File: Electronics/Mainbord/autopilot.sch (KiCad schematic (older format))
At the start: 49 parts

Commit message: Electronics - Misc works
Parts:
- added R? (x7): 270, symbol Device:R_Small
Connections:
- net ALT_LED: now also R?.1; no longer U?.12 (O7)
- net APP_LED: no longer U?.15 (O4)
- net AP_A_LED: no longer U?.17 (O2)
- net AP_B_LED: no longer U?.16 (O3)
- net ARM_L_LED: now also R?.1; no longer U?.18 (O1)
- net ARM_R_LED: no longer U?.18 (O1)
- net BANK_LED: no longer U?.14 (O5)
- net BC_LED: no longer U?.12 (O7)
- net BOTTLE_R_LED: no longer U?.14 (O5)
- net CO_LED: no longer U?.16 (O3)
- net DEPLOY_L_LED: now also R?.1; no longer U?.16 (O3)
- net DEPLOY_R_LED: no longer U?.16 (O3)
- net ENG_FIRE_R_LED: no longer U?.15 (O4)
- net FLC_LED: now also R?.1; no longer U?.11 (O8)
- net HDG_LED: now also R?.1; no longer U?.13 (O6)
- net MAV_LED: now also R?.1; no longer U?.18 (O1)
- net MT_A_LED: no longer U?.13 (O6)
- net MT_B_LED: no longer U?.12 (O7)
- net PFD_L_LED: no longer U?.11 (O8)
- net PFD_R_LED: no longer U?.10 (COM)
- net SPD_LED: no longer U?.18 (O1)
- net STBY_LED: no longer U?.11 (O8)
- net UNLOCK_L_LED: now also R?.1; no longer U?.17 (O2), U?.17 (O2)
- net VNAV_LED: no longer U?.17 (O2)
- net VS_LED: no longer U?.13 (O6)
- net YD_A_LED: no longer U?.15 (O4)
- net YD_B_LED: no longer U?.14 (O5)
- new net: R?.2, U?.18 (O1) (x2)
- new net: R?.2, U?.17 (O2)
- new net: R?.2, U?.16 (O3)
- new net: R?.2, U?.13 (O6)
- new net: R?.2, U?.12 (O7)
- new net: R?.2, U?.11 (O8)
- no-connect marks 3 -> 7
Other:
- note added: "Power the LEDs with 5V\nThe big PB do not need a resistor\nAP PB can go up to 12 mA Vd = ?\nOrange LEDs can go up to Vd = ?\nLEDs in paralell. 50% max current each (if one dies, the other take the load)"
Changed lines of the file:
@@
 EESchema Schematic File Version 4
-LIBS:CitationX_cockpit-cache
-EELAYER 26 0
+EELAYER 30 0
 EELAYER END
 $Descr A3 11693 16535 portrait
 encoding utf-8
-Sheet 10 7
+Sheet 7 7
 Title ""
 Date ""
@@
 	0    -1   -1   0
 $EndComp
-Text Label 6050 1850 0    50   ~ 0
+Text Label 6250 1850 0    50   ~ 0
 HDG_LED
-Text Label 6050 1950 0    50   ~ 0
+Text Label 6250 1950 0    50   ~ 0
 ALT_LED
-Text Label 6050 2050 0    50   ~ 0
+Text Label 6250 2050 0    50   ~ 0
 FLC_LED
 Wire Wire Line
 	900  2050 850  2050
-Text Label 6050 3350 0    50   ~ 0
+Text Label 6250 3350 0    50   ~ 0
 MAV_LED
-Text Label 6050 3450 0    50   ~ 0
+Text Label 6250 3450 0    50   ~ 0
 VNAV_LED
-Text Label 6050 3550 0    50   ~ 0
+Text Label 6250 3550 0    50   ~ 0
 CO_LED
-Text Label 6050 3650 0    50   ~ 0
+Text Label 6250 3650 0    50   ~ 0
 APP_LED
-Text Label 6050 3750 0    50   ~ 0
+Text Label 6250 3750 0    50   ~ 0
 BANK_LED
-Text Label 6050 3850 0    50   ~ 0
+Text Label 6250 3850 0    50   ~ 0
 VS_LED
 Text GLabel 1850 2250 0    50   Input ~ 0
@@
 Text GLabel 4450 1550 0    50   Input ~ 0
 CLK
-Text Label 6050 3950 0    50   ~ 0
+Text Label 6250 3950 0    50   ~ 0
 BC_LED
-Text Label 6050 4050 0    50   ~ 0
+Text Label 6250 4050 0    50   ~ 0
 STBY_LED
-Text Label 6050 5450 0    50   ~ 0
+Text Label 6200 5450 0    50   ~ 0
 AP_A_LED
-Text Label 6050 5550 0    50   ~ 0
+Text Label 6200 5550 0    50   ~ 0
 AP_B_LED
-Text Label 6050 5650 0    50   ~ 0
+Text Label 6200 5650 0    50   ~ 0
 YD_A_LED
-Text Label 6050 5750 0    50   ~ 0
+Text Label 6200 5750 0    50   ~ 0
 YD_B_LED
-Text Label 6050 5350 0    50   ~ 0
+Text Label 6200 5350 0    50   ~ 0
 SPD_LED
 Text GLabel 1850 3950 0    50   Input ~ 0
@@
 	0    -1   -1   0
 $EndComp
-Text Label 6050 5850 0    50   ~ 0
+Text Label 6200 5850 0    50   ~ 0
 MT_A_LED
-Text Label 6050 5950 0    50   ~ 0
+Text Label 6200 5950 0    50   ~ 0
 MT_B_LED
 Text GLabel 1850 5650 0    50   Input ~ 0
@@
 Text Label 1300 1550 0    50   ~ 0
 BOTTLE_L
-Text Label 6050 1350 0    50   ~ 0
+Text Label 6250 1350 0    50   ~ 0
 ARM_L_LED
-Text Label 6050 1450 0    50   ~ 0
+Text Label 6250 1450 0    50   ~ 0
 UNLOCK_L_LED
-Text Label 6050 1550 0    50   ~ 0
+Text Label 6250 1550 0    50   ~ 0
 DEPLOY_L_LED
-Text Label 6050 1650 0    50   ~ 0
+Text Label 6250 1650 0    50   ~ 0
 ENG_FIRE_L_LED
-Text Label 6050 1750 0    50   ~ 0
+Text Label 6250 1750 0    50   ~ 0
 BOTTLE_L_LED
-Text Label 6600 7250 0    50   ~ 0
+Text Label 6850 7350 0    50   ~ 0
 PFD_R_LED
-Text Label 6050 6050 0    50   ~ 0
+Text Label 6200 6050 0    50   ~ 0
 PFD_L_LED
 $Comp
@@
 Wire Wire Line
 	5250 6700 5250 6250
-Text Label 6600 7350 0    50   ~ 0
+Text Label 6850 7450 0    50   ~ 0
 ARM_R_LED
-Text Label 6600 7450 0    50   ~ 0
+Text Label 6850 7550 0    50   ~ 0
 UNLOCK_L_LED
-Text Label 6600 7550 0    50   ~ 0
+Text Label 6850 7650 0    50   ~ 0
 DEPLOY_R_LED
-Text Label 6600 7650 0    50   ~ 0
+Text Label 6850 7750 0    50   ~ 0
 ENG_FIRE_R_LED
-Text Label 6600 7750 0    50   ~ 0
+Text Label 6850 7850 0    50   ~ 0
 BOTTLE_R_LED
 $Comp
@@
 Wire Wire Line
 	5800 7350 5250 7350
+Text Notes 8150 3400 0    50   ~ 0
+Power the LEDs with 5V\nThe big PB do not need a resistor\nAP PB can go up to 12 mA Vd = ?\nOrange LEDs can go up to Vd = ?\nLEDs in paralell. 50% max current each (if one dies, the other take the load)
+$Comp
+L Device:R_Small R?
+U 1 1 5DF27DDD
+P 6150 1350
+F 0 "R?" V 6100 1300 20  0000 C CNN
+F 1 "270" V 6150 1350 20  0000 C CNN
+F 2 "" H 6150 1350 50  0001 C CNN
+F 3 "~" H 6150 1350 50  0001 C CNN
+	1    6150 1350
+	0    1    1    0
+$EndComp
+$Comp
+L Device:R_Small R?
+U 1 1 5DF2C1C9
+P 6150 1450
+F 0 "R?" V 6100 1400 20  0000 C CNN
+F 1 "270" V 6150 1450 20  0000 C CNN
+F 2 "" H 6150 1450 50  0001 C CNN
+F 3 "~" H 6150 1450 50  0001 C CNN
+	1    6150 1450
+	0    1    1    0
+$EndComp
+$Comp
+L Device:R_Small R?
+U 1 1 5DF2C41C
+P 6150 1550
+F 0 "R?" V 6100 1500 20  0000 C CNN
+F 1 "270" V 6150 1550 20  0000 C CNN
+F 2 "" H 6150 1550 50  0001 C CNN
+F 3 "~" H 6150 1550 50  0001 C CNN
+	1    6150 1550
+	0    1    1    0
+$EndComp
+Wire Wire Line
+	6050 1650 6250 1650
+Wire Wire Line
+	6050 1750 6250 1750
+$Comp
+L Device:R_Small R?
+U 1 1 5DF3257F
+P 6150 1850
+F 0 "R?" V 6100 1800 20  0000 C CNN
+F 1 "270" V 6150 1850 20  0000 C CNN
+F 2 "" H 6150 1850 50  0001 C CNN
+F 3 "~" H 6150 1850 50  0001 C CNN
+	1    6150 1850
+	0    1    1    0
+$EndComp
+$Comp
+L Device:R_Small R?
+U 1 1 5DF32A59
+P 6150 1950
+F 0 "R?" V 6100 1900 20  0000 C CNN
+F 1 "270" V 6150 1950 20  0000 C CNN
+F 2 "" H 6150 1950 50  0001 C CNN
+F 3 "~" H 6150 1950 50  0001 C CNN
+	1    6150 1950
+	0    1    1    0
+$EndComp
+$Comp
+L Device:R_Small R?
+U 1 1 5DF32D0A
+P 6150 2050
+F 0 "R?" V 6100 2000 20  0000 C CNN
+F 1 "270" V 6150 2050 20  0000 C CNN
+F 2 "" H 6150 2050 50  0001 C CNN
+F 3 "~" H 6150 2050 50  0001 C CNN
+	1    6150 2050
+	0    1    1    0
+$EndComp
+$Comp
+L Device:R_Small R?
+U 1 1 5DF346A4
+P 6150 3350
+F 0 "R?" V 6150 3300 20  0000 C CNN
+F 1 "270" V 6150 3350 20  0000 C CNN
+F 2 "" H 6150 3350 50  0001 C CNN
+F 3 "~" H 6150 3350 50  0001 C CNN
+	1    6150 3350
+	0    1    1    0
+$EndComp
+NoConn ~ 6050 5250
+NoConn ~ 6050 3250
+NoConn ~ 6050 1250
+NoConn ~ 6600 7250
 $EndSCHEMATC

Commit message: Electronics - Minor changes
Resistors to LEDs, transistors
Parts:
- removed D? (x8): LED_Small, symbol Device:LED_Small
- removed R? (x2): 150, symbol Device:R_Small
- removed R? (x7): 270, symbol Device:R_Small
- removed U? (x16): PB86-A1, symbol adessein:PB86-A1
- added R? (x25): R, symbol Device:R
- gave numbers to parts that had none: 23
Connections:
- net +3V3: now also J31.10 (Pin_10)
- net ALT_LED: now also R?.1
- net APP_LED: now also R?.1
- net AP_A_LED: now also R?.1
- net AP_B_LED: now also R?.1
- net ARM_L_LED: now also R?.1
- net ARM_R_LED: now also R?.1
- net BANK_LED: now also R?.1
- net BC_LED: now also R?.1
- net BOTTLE_R_LED: now also U69.13 (O6)
- net CO_LED: now also R?.1
- net DEPLOY_L_LED: now also R?.1
- net DEPLOY_R_LED: now also U69.15 (O4)
- net ENG_FIRE_R_LED: now also U69.14 (O5)
- net FLC_LED: now also R?.1
- net HDG_LED: now also R?.1
- net MAV_LED: now also R?.1
- net MT_A_LED: now also R?.1
- net MT_B_LED: now also R?.1
- net PFD_L_LED: now also R?.1
- net PFD_R_LED: now also R?.1
- net SPD_LED: now also R?.1
- net STBY_LED: now also R?.1
- net UNLOCK_L_LED: now also R?.1, R?.1
- net VNAV_LED: now also R?.1
- net VS_LED: now also R?.1
- net YD_A_LED: now also R?.1
- net YD_B_LED: now also R?.1
- net at U66.18 (O1): now also R?.2
- net at U66.17 (O2): now also R?.2
- net at U66.16 (O3): now also R?.2
- net at U66.13 (O6): now also R?.2
- net at U66.12 (O7): now also R?.2
- net at U66.11 (O8): now also R?.2
- net at U67.18 (O1): now also R?.2
- net at U69.16 (O3): now also R?.2
- net at U69.17 (O2): now also R?.2
- net at U69.18 (O1): now also R?.2
- net at U67.11 (O8): now also R?.2
- net at U67.12 (O7): now also R?.2
- net at U67.13 (O6): now also R?.2
- net at U67.14 (O5): now also R?.2
- net at U67.15 (O4): now also R?.2
- net at U67.16 (O3): now also R?.2
- net at U67.17 (O2): now also R?.2
- net at U68.11 (O8): now also R?.2
- net at U68.12 (O7): now also R?.2
- net at U68.13 (O6): now also R?.2
- net at U68.14 (O5): now also R?.2
- net at U68.15 (O4): now also R?.2
- net at U68.16 (O3): now also R?.2
- net at U68.17 (O2): now also R?.2
- net at U68.18 (O1): now also R?.2
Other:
- note added: "Check that 3.3V without resistor is enough for the push buttons"
- note removed: "Power the LEDs with 5V\nThe big PB do not need a resistor\nAP PB can go up to 12 mA Vd = ?\nOrange LEDs can go up to Vd = ?\nLEDs in paralell. 50% max current each (if one dies, the other take the load)"

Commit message: Electronics - Misc works
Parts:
- removed R? (x21): R, symbol Device:R
- added R? (x19): 1.5k, symbol Device:R
- added R? (x3): 47, symbol Device:R
- R? (x3): value R -> 47
- R?: value R -> 1.5k
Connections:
- net BOTTLE_T_LED is gone; now on net BOTTLE_R_LED: J31.6 (Pin_6)
- net ALT_LED: now also R?.1
- net APP_LED: now also R?.1
- net AP_A_LED: now also R?.1
- net AP_B_LED: now also R?.1
- net ARM_R_LED: now also R?.1
- net BANK_LED: now also R?.1
- net BC_LED: now also R?.1
- net CO_LED: now also R?.1
- net DEPLOY_R_LED: now also R?.1; no longer U69.15 (O4)
- net FLC_LED: now also R?.1
- net MAV_LED: now also R?.1
- net MT_A_LED: now also R?.1
- net MT_B_LED: now also R?.1
- net PFD_L_LED: now also R?.1
- net PFD_R_LED: now also R?.1
- net SPD_LED: now also R?.1
- net STBY_LED: now also R?.1
- net UNLOCK_L_LED: now also R?.1
- net VNAV_LED: now also R?.1
- net VS_LED: now also R?.1
- net YD_A_LED: now also R?.1
- net YD_B_LED: now also R?.1
- net at U66.12 (O7): now also R?.2
- net at U66.11 (O8): now also R?.2
- net at U67.18 (O1): now also R?.2
- net at U67.17 (O2): now also R?.2
- net at U67.16 (O3): now also R?.2
- net at U67.15 (O4): now also R?.2
- net at U67.14 (O5): now also R?.2
- net at U67.13 (O6): now also R?.2
- net at U67.12 (O7): now also R?.2
- net at U67.11 (O8): now also R?.2
- net at U68.18 (O1): now also R?.2
- net at U68.17 (O2): now also R?.2
- net at U68.16 (O3): now also R?.2
- net at U68.15 (O4): now also R?.2
- net at U68.14 (O5): now also R?.2
- net at U68.13 (O6): now also R?.2
- net at U68.12 (O7): now also R?.2
- net at U68.11 (O8): now also R?.2
- net at U69.18 (O1): now also R?.2
- net at U69.17 (O2): now also R?.2
- net at U69.16 (O3): now also R?.2
- new net: R?.2, U69.15 (O4)
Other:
- note removed: "Check that 3.3V without resistor is enough for the push buttons"

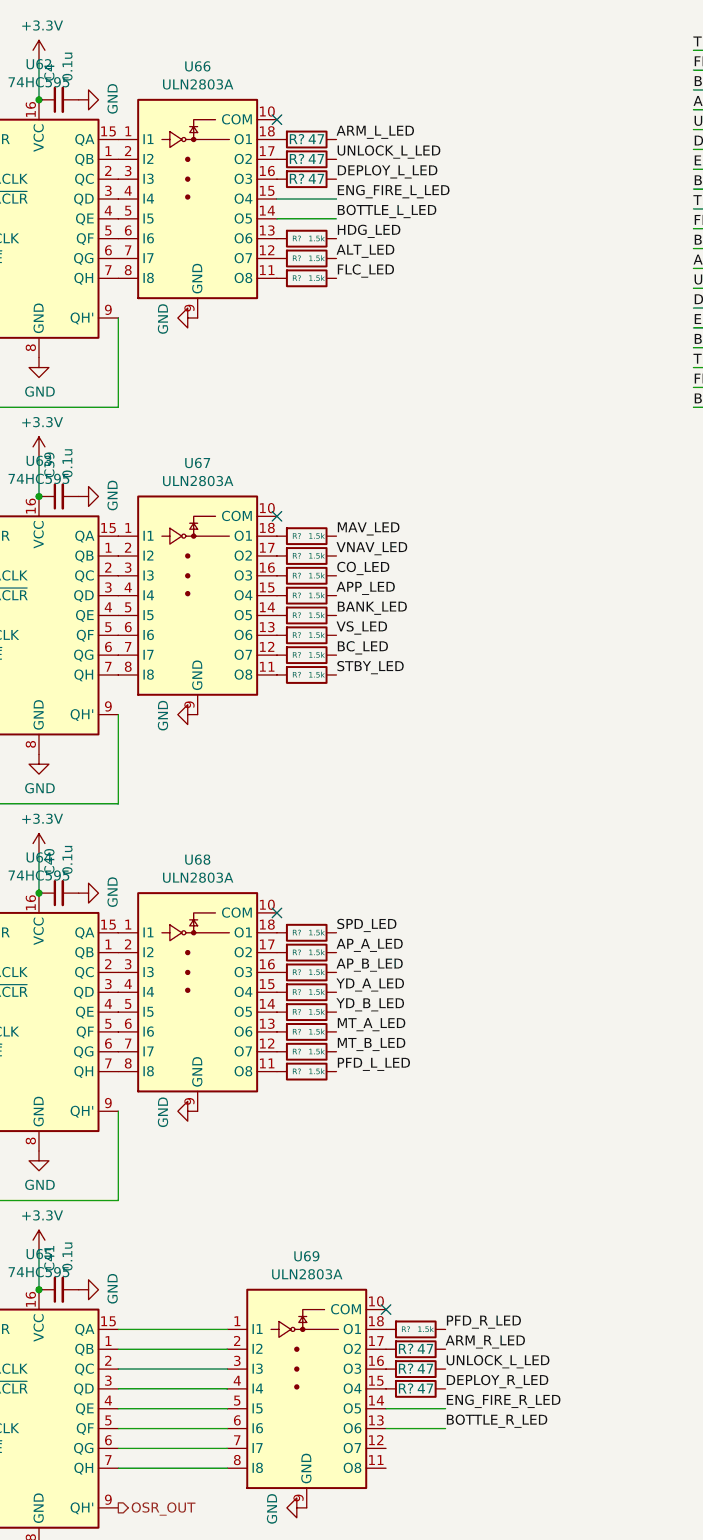
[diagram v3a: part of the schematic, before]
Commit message: Electronics - Adds LCSC part numbers and footprints
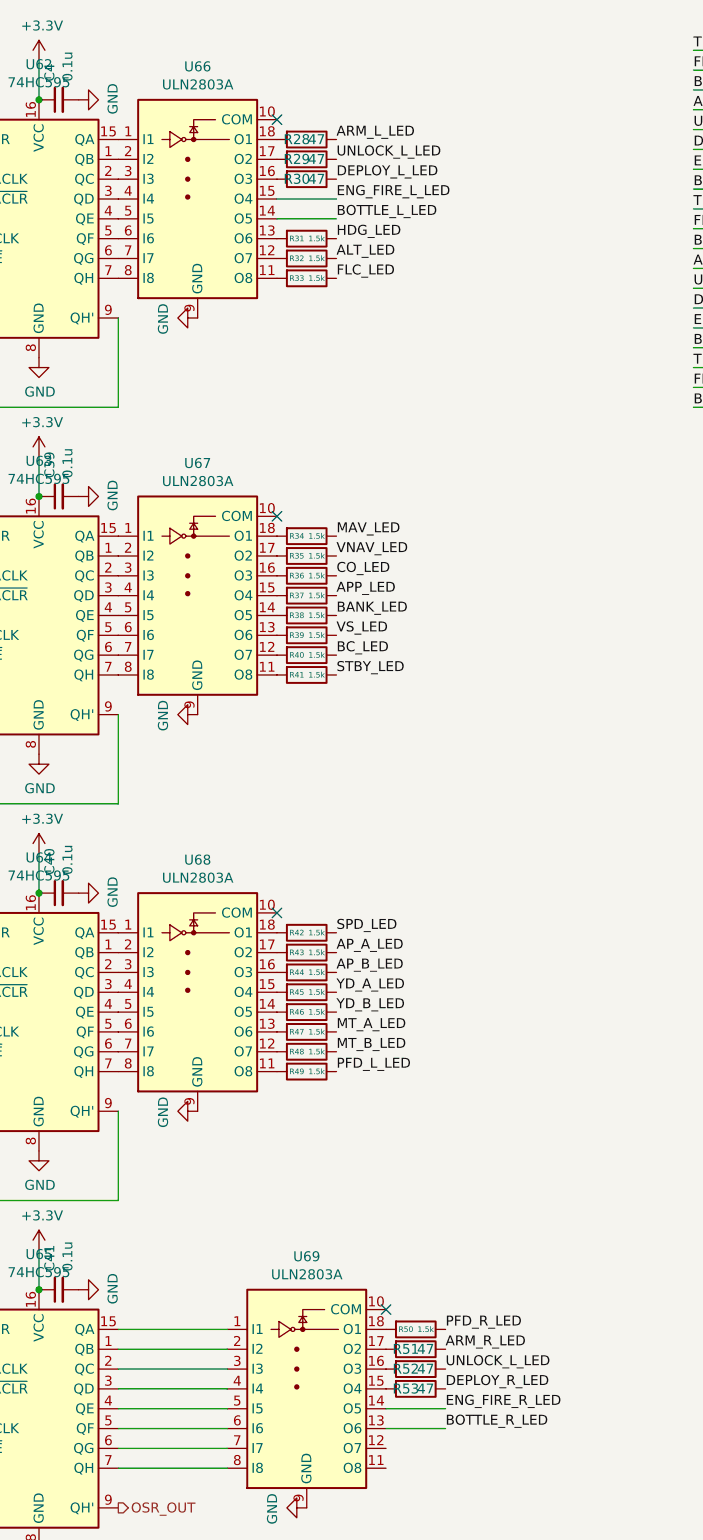
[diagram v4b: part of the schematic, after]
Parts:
- U32, U33, U41, U62, U63, U64, U65: footprint (none) -> Package_SO:SOIC-16_3.9x9.9mm_P1.27mm; LCSC (none) -> C5947
- U66, U67, U68, U69: footprint (none) -> Package_SO:SOIC-18W_7.5x11.6mm_P1.27mm; LCSC (none) -> C9683
- gave numbers to parts that had none: 26
